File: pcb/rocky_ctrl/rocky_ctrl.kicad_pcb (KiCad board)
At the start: 4 copper layers, 156 x 155.6 mm, 173 parts, among them J1 XT60PW-M, J10 STEMMA QT, J11 IMU INT/RST, J12 SPARE, J2 Pi 5V, J3 USB-C, J4 Pi GPIO 5-14, J5 LEG1, J6 LEG2, J7 LEG3, J8 LEG4, J9 LEG5, Q1 BSC030P03NS3, Q2 BSC030P03NS3, Q3 MMBT3904, Q4 2N7002, Q5 MMBT3904, Q6 MMBT3904, Q7 2N7002, Q8 2N7002, SW1 EN, SW2 BOOT, U1 INA180A3, U10 SN74LV1T126, U11 SN74LV1T125, U2 TPS54560B, U3 AP63203WU, U4 USBLC6-2SC6, U5 CH340C, U6 74LVC1G3157, U7 ESP32-WROOM-32E-N8, U8 SN74LV1T126, U9 SN74LV1T125

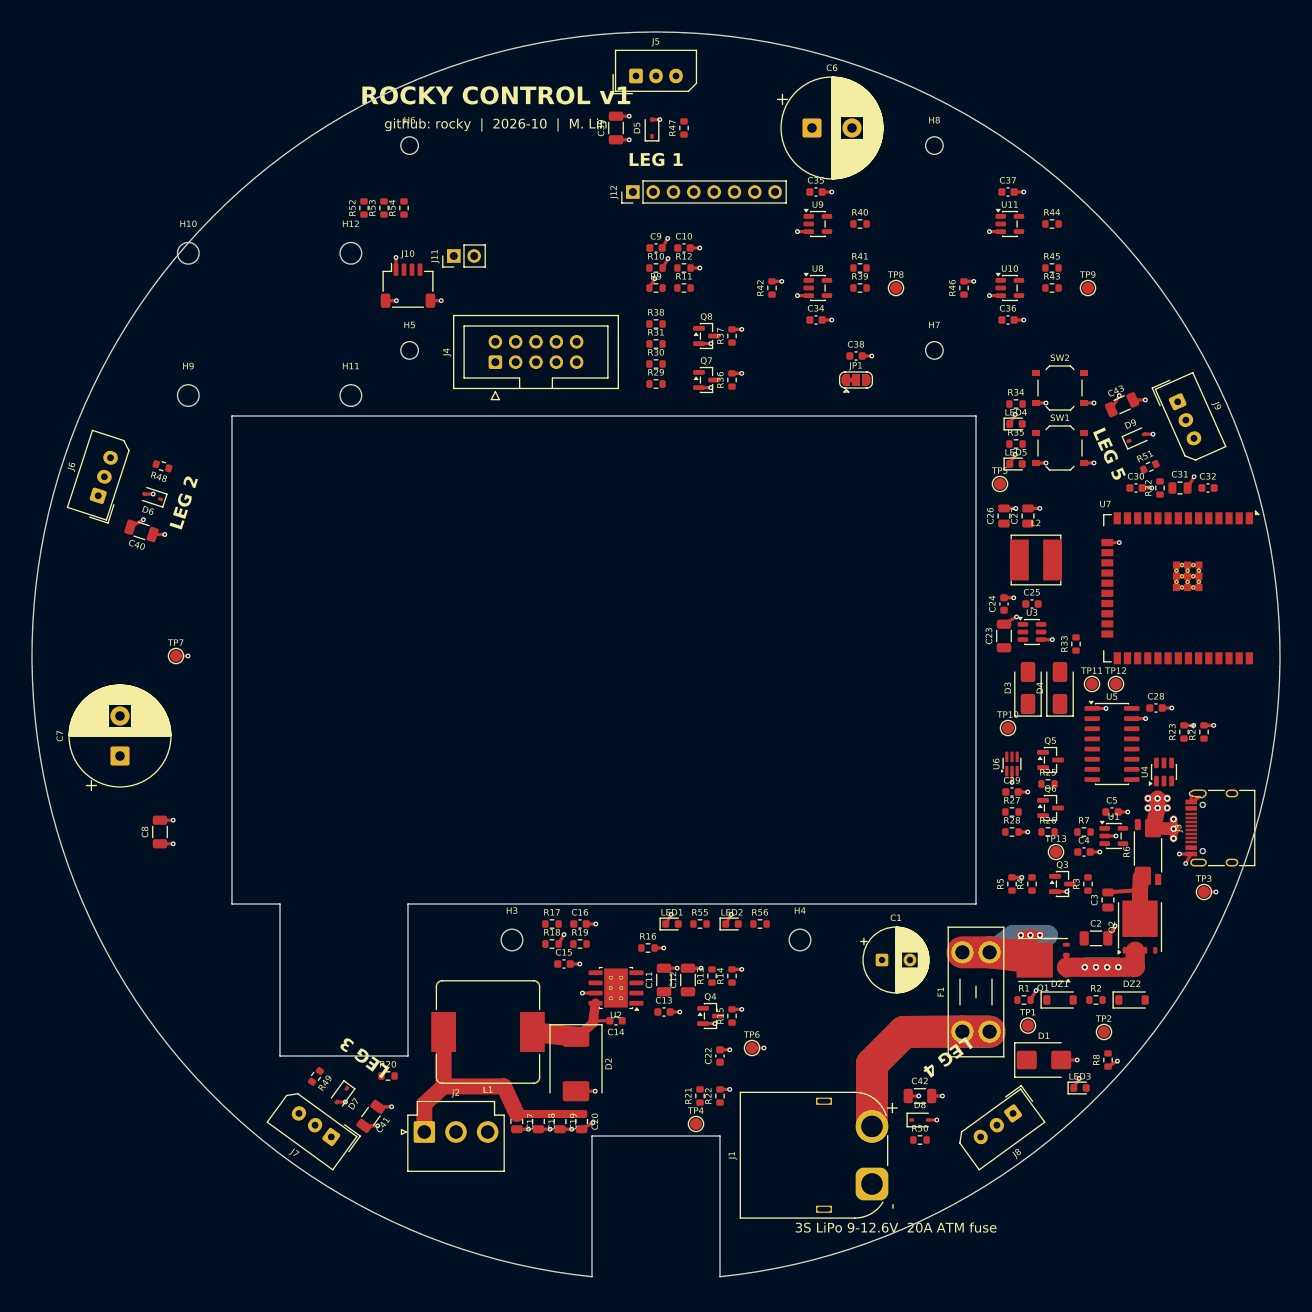
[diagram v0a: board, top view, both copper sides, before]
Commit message: Control PCB v1: routed 4-layer ring board, ERC/DRC clean, STEP and JLCPCB fab outputs
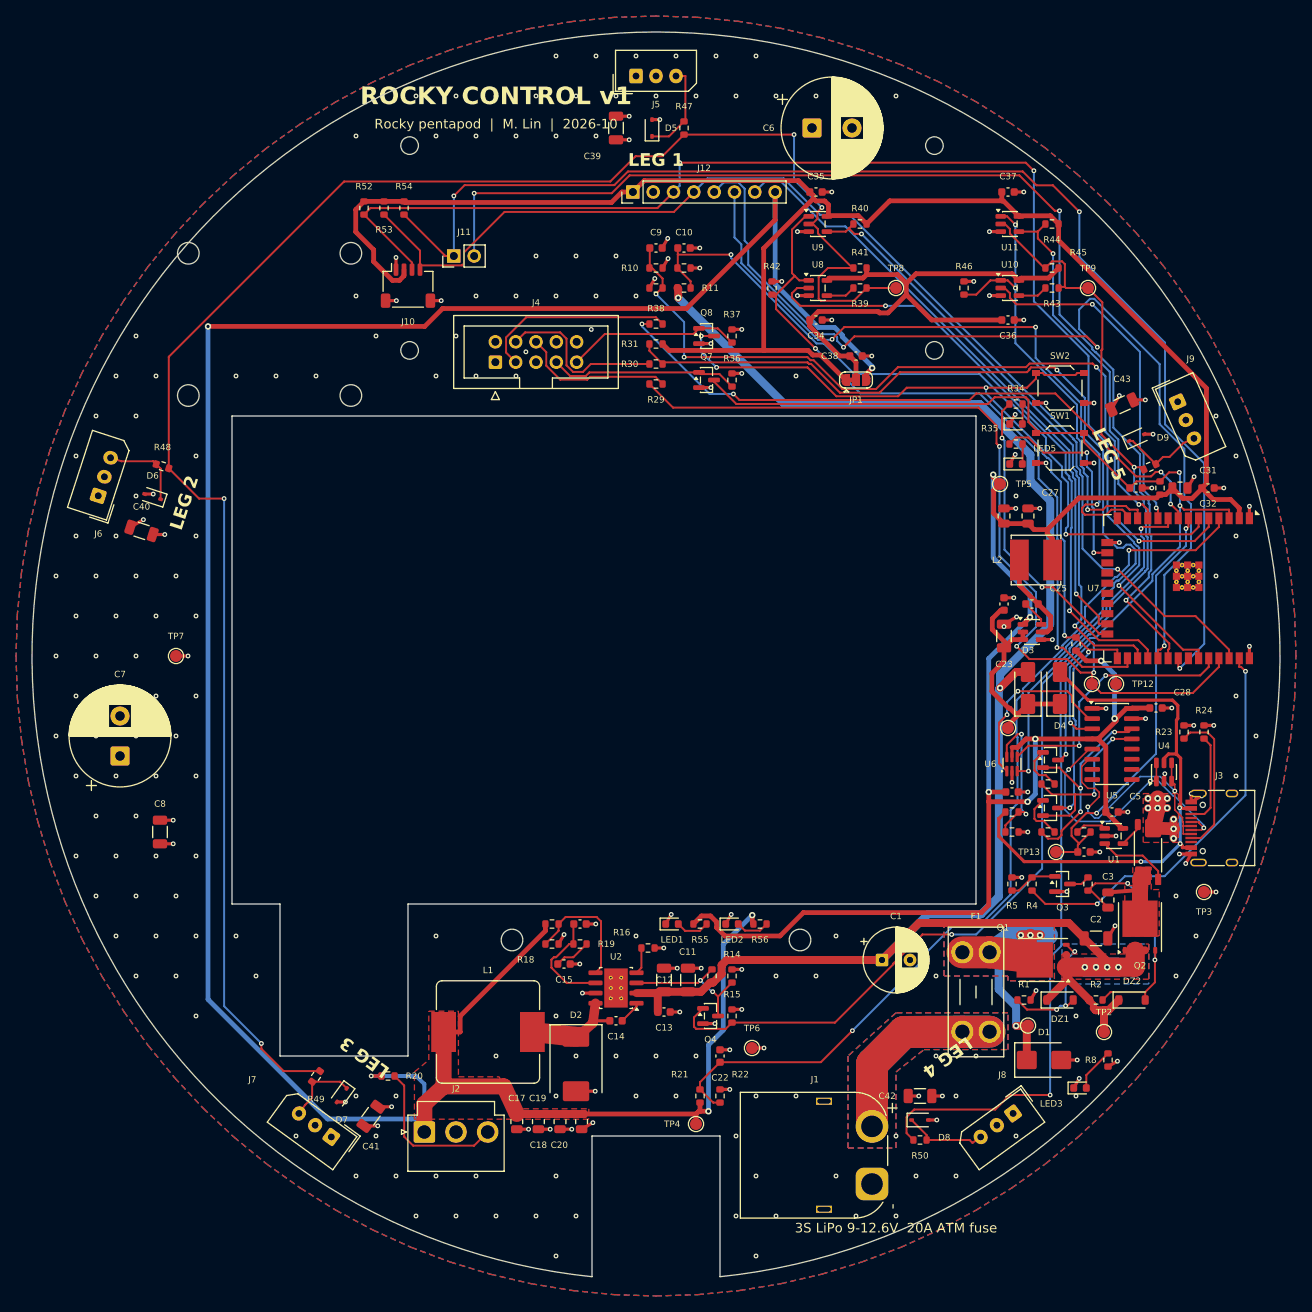
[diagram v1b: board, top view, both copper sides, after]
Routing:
- net +3V3: track 0.00 -> 403.3 mm, vias 0 -> 7
- net +5V: track 33.0 -> 340.8 mm, vias 0 -> 5
- net /BUSA: track 0.00 -> 230.9 mm, vias 0 -> 4
- net /VBAT_P: track 19.9 -> 239.5 mm, vias 4 -> 6
- net /SDA: track 0.00 -> 170.7 mm, vias 0 -> 3
- net /IMU_INT: track 0.00 -> 163.6 mm, vias 0 -> 3
- net /BUSB: track 0.00 -> 150.7 mm, vias 0 -> 2
- net /IMU_RST: track 0.00 -> 148.1 mm, vias 0 -> 3
- net /SCL: track 0.00 -> 148.1 mm, vias 0 -> 1
- net /ESP_TX0: track 0.00 -> 125.7 mm, vias 0 -> 4
- net /GPIO5: track 0.00 -> 123.6 mm, vias 0 -> 3
- net /BOOT: track 0.00 -> 121.6 mm, vias 0 -> 6
- net /PI_TXD: track 0.00 -> 118.5 mm, vias 0 -> 2
- net /EN: track 0.00 -> 118.4 mm, vias 0 -> 3
- net /V5_SENSE: track 0.00 -> 115.9 mm, vias 0 -> 2
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- added copper zone on F.Cu, net +5V
- added copper zone on B.Cu, net /VBAT_F
- added copper zone on F.Cu, net /VBAT_F
- added copper zone on B.Cu, net /VBAT_IN
- added copper zone on F.Cu, net /VBAT_IN
- added copper zone on B.Cu, net /VBAT_P
- added copper zone on F.Cu, net /VBAT_P
- added copper zone on F.Cu, net /VSERVO
- added copper zone on In2.Cu, net /VSERVO
- added copper zone on F.Cu, net /VSERVO_SW
- added copper zone on B.Cu, net GND
- added copper zone on F.Cu, net GND
- added copper zone on In1.Cu, net GND
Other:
- board text added: "Rocky pentapod | M. Lin | 2026-10"
- board text removed: "github: rocky | 2026-10 | M. Lin"
